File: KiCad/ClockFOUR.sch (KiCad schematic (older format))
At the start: 64 parts, among them P1 ICSP, P10 Marquee, P2 FTDI, P5 BARREL_JACK, P6 5VEN_L, P7 I2C_L, P8 5VEN_R, P9 I2C_R, SW1 SW_RST, SW2 SW_L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

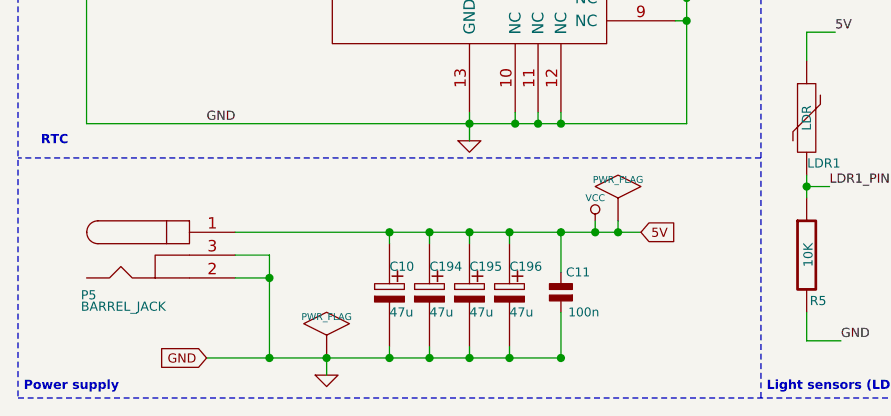
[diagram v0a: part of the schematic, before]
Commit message: C4 rev2 aka Chronogram, Sch and PCB mods, revised BoM
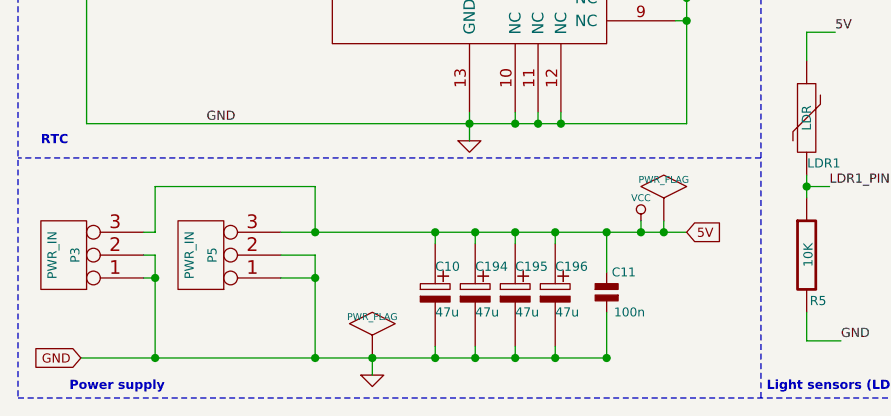
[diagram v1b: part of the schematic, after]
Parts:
- removed P5: BARREL_JACK, C4_Pretty:JACK_PJ-047a, symbol BARREL_JACK
- added P3, P5: PWR_IN, C4_Pretty:Header_3x1_PWR, symbol CONN_3
- S10, S11, S12, S13: footprint C4_Pretty:Screw_2mm -> C4_Pretty:Slot_tiewrap
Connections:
- net GND: now also P3.1, P3.2, P5.1, P5.2
- net VCC: now also P3.3, P5.3
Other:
- moved on the sheet: C10, C11, C194, C195, C196

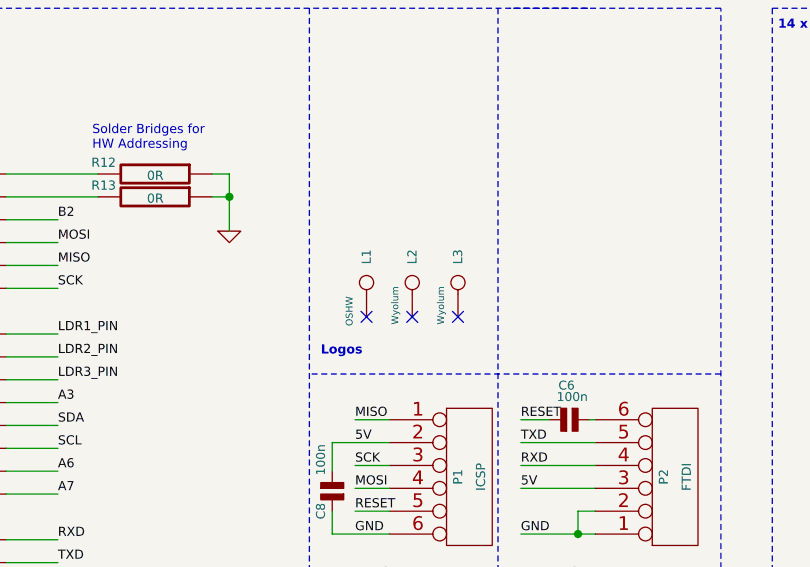
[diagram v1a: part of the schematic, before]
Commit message: Minor board tweaks
Trying to add a logo to the back of the board
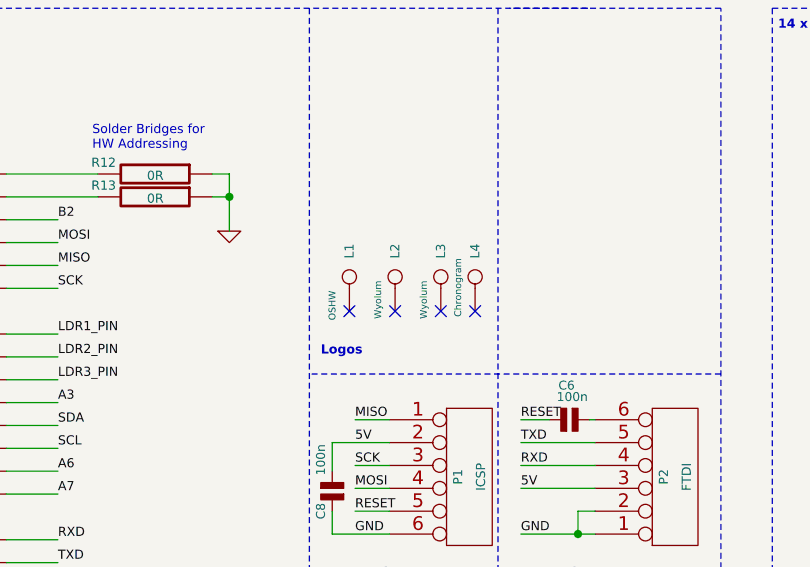
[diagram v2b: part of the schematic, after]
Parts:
- added L4: Chronogram, C4_Pretty:chronogram_dot, symbol CONN_1
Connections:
- no-connect marks 12 -> 13
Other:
- moved on the sheet: L1, L2, L3
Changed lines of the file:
@@
 C1 ED 35 72 E0 F7 FB FF F1 1F FF F1 9F FF F9 9F C7 C7 C7 73 1A 9F 2B 70 38 1C FB F6 ED 3B 79 F2
 E4 23 8F 3C 52 B0 F1 D9 2E 76 F1 FF 03 17 ED 19 47 28 92 59 FB 00 00 00 00 49 45 4E 44 AE 42 60
-82 24
+82 00
 EndData
 $EndBitmap
-NoConn ~ 5125 1900
-NoConn ~ 5325 1900
+NoConn ~ 5050 1875
+NoConn ~ 5250 1875
 $Comp
 L CONN_1 L1
 U 1 1 511CD9F8
-P 5125 1750
-F 0 "L1" H 5205 1750 40  0000 L CNN
-F 1 "OSHW" H 5000 1825 30  0000 C CNN
-F 2 "C4_Pretty:Logo_silk_OSHW_6x6mm" H 5125 1905 30  0001 C CNN
-F 3 "" H 5125 1750 60  0001 C CNN
-	1    5125 1750
+P 5050 1725
+F 0 "L1" H 5130 1725 40  0000 L CNN
+F 1 "OSHW" H 4925 1800 30  0000 C CNN
+F 2 "C4_Pretty:Logo_silk_OSHW_6x6mm" H 5050 1880 30  0001 C CNN
+F 3 "" H 5050 1725 60  0001 C CNN
+	1    5050 1725
 	0    -1   -1   0
 $EndComp
@@
 L CONN_1 L2
 U 1 1 511CD9F5
-P 5325 1750
-F 0 "L2" H 5405 1750 40  0000 L CNN
-F 1 "Wyolum" H 5225 1825 30  0000 C CNN
-F 2 "C4_Pretty:Logo-WL3" H 5250 1825 30  0001 C CNN
-F 3 "" H 5325 1750 60  0001 C CNN
-	1    5325 1750
+P 5250 1725
+F 0 "L2" H 5330 1725 40  0000 L CNN
+F 1 "Wyolum" H 5150 1800 30  0000 C CNN
+F 2 "C4_Pretty:Logo-WL3" H 5175 1800 30  0001 C CNN
+F 3 "" H 5250 1725 60  0001 C CNN
+	1    5250 1725
 	0    -1   -1   0
 $EndComp
@@
 $EndSheet
 $Comp
-L GND #PWR01
+L GND #PWR1
 U 1 1 50E7FAEA
 P 2200 7325
-F 0 "#PWR01" H 2200 7325 30  0001 C CNN
+F 0 "#PWR1" H 2200 7325 30  0001 C CNN
 F 1 "GND" H 2200 7255 30  0001 C CNN
 F 2 "" H 2200 7325 60  0001 C CNN
@@
 $EndComp
 $Comp
-L GND #PWR02
+L GND #PWR2
 U 1 1 542A3CA4
 P 2600 3975
-F 0 "#PWR02" H 2600 3975 30  0001 C CNN
+F 0 "#PWR2" H 2600 3975 30  0001 C CNN
 F 1 "GND" H 2600 3905 30  0001 C CNN
 F 2 "" H 2600 3975 60  0000 C CNN
@@
 SCL
 $Comp
-L GND #PWR03
+L GND #PWR3
 U 1 1 542BA28D
 P 2625 6300
-F 0 "#PWR03" H 2625 6300 30  0001 C CNN
+F 0 "#PWR3" H 2625 6300 30  0001 C CNN
 F 1 "GND" H 2625 6230 30  0001 C CNN
 F 2 "" H 2625 6300 60  0000 C CNN
@@
 RESET
 $Comp
-L PWR_FLAG #FLG04
+L PWR_FLAG #FLG1
 U 1 1 542A828E
 P 950 4450
-F 0 "#FLG04" H 950 4720 30  0001 C CNN
+F 0 "#FLG1" H 950 4720 30  0001 C CNN
 F 1 "PWR_FLAG" H 950 4680 30  0000 C CNN
 F 2 "" H 950 4450 60  0000 C CNN
@@
 SCK
 $Comp
-L PWR_FLAG #FLG05
+L PWR_FLAG #FLG3
 U 1 1 542C2187
 P 3475 6650
-F 0 "#FLG05" H 3475 6745 30  0001 C CNN
+F 0 "#FLG3" H 3475 6745 30  0001 C CNN
 F 1 "PWR_FLAG" H 3475 6830 30  0000 C CNN
 F 2 "" H 3475 6650 60  0000 C CNN
@@
 $EndComp
 $Comp
-L PWR_FLAG #FLG06
+L PWR_FLAG #FLG2
 U 1 1 542C219E
 P 2200 7250
-F 0 "#FLG06" H 2200 7345 30  0001 C CNN
+F 0 "#FLG2" H 2200 7345 30  0001 C CNN
 F 1 "PWR_FLAG" H 2200 7430 30  0000 C CNN
 F 2 "" H 2200 7250 60  0000 C CNN
@@
 $EndComp
 $Comp
-L VCC #PWR07
+L VCC #PWR4
 U 1 1 542BE803
 P 3375 6650
-F 0 "#PWR07" H 3375 6750 30  0001 C CNN
+F 0 "#PWR4" H 3375 6750 30  0001 C CNN
 F 1 "VCC" H 3375 6750 30  0000 C CNN
 F 2 "" H 3375 6650 60  0000 C CNN
@@
 Text Label 5625 4900 2    40   ~ 0
 SW_R
-NoConn ~ 5525 1900
+NoConn ~ 5450 1875
 $Comp
 L CONN_1 L3
 U 1 1 5439906B
-P 5525 1750
-F 0 "L3" H 5605 1750 40  0000 L CNN
-F 1 "Wyolum" H 5425 1825 30  0000 C CNN
-F 2 "C4_Pretty:Logo-WL3" H 5450 1825 30  0001 C CNN
-F 3 "" H 5525 1750 60  0001 C CNN
-	1    5525 1750
+P 5450 1725
+F 0 "L3" H 5530 1725 40  0000 L CNN
+F 1 "Wyolum" H 5350 1800 30  0000 C CNN
+F 2 "C4_Pretty:Logo-WL3" H 5375 1800 30  0001 C CNN
+F 3 "" H 5450 1725 60  0001 C CNN
+	1    5450 1725
 	0    -1   -1   0
 $EndComp
@@
 $EndComp
 $Comp
-L GND #PWR08
+L GND #PWR5
 U 1 1 5439D79A
 P 4525 1525
-F 0 "#PWR08" H 4525 1525 30  0001 C CNN
+F 0 "#PWR5" H 4525 1525 30  0001 C CNN
 F 1 "GND" H 4525 1455 30  0001 C CNN
 F 2 "" H 4525 1525 60  0000 C CNN
@@
 	1950 6500 1950 6700
 Connection ~ 1950 6700
+NoConn ~ 5600 1875
+$Comp
+L CONN_1 L4
+U 1 1 54C81555
+P 5600 1725
+F 0 "L4" H 5680 1725 40  0000 L CNN
+F 1 "Chronogram" H 5425 1800 30  0000 L CNN
+F 2 "C4_Pretty:chronogram_dot" H 5600 1880 30  0001 C CNN
+F 3 "" H 5600 1725 60  0001 C CNN
+	1    5600 1725
+	0    -1   -1   0
+$EndComp
 $EndSCHEMATC

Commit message: Added Fuse/Zener protection, silk legend mods
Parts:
- added D1: SMBJ5339B, C4_Pretty:diode-DO214AA, symbol DIODE_ZENER
- added F1: miniSMDC200F/16, C4_Pretty:f_1812, symbol FUSE
- L1, L2, L3: symbol CONN_1 -> Logos
- L4: footprint C4_Pretty:chronogram_dot -> C4_Pretty:Logo_silk_OSHW_6x6mm; symbol CONN_1 -> Logos
- LDR1, LDR2, LDR3: footprint C4_Pretty:r_0805 -> C4_Pretty:r_0805_ldr
- SW2: Label (none) -> Mode
- SW3: Label (none) -> Color
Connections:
- net GND: now also D1.1 (A)
- net VCC: now also D1.2 (K), F1.2; no longer P3.3, P5.3
- new net: F1.1, P3.3, P5.3
- no-connect marks 13 -> 9
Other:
- moved on the sheet: P3, P5
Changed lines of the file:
@@
 EESchema Schematic File Version 2
 LIBS:ClockFOUR
+LIBS:device
 LIBS:ClockFOUR-cache
 EELAYER 25 0
@@
 C1 ED 35 72 E0 F7 FB FF F1 1F FF F1 9F FF F9 9F C7 C7 C7 73 1A 9F 2B 70 38 1C FB F6 ED 3B 79 F2
 E4 23 8F 3C 52 B0 F1 D9 2E 76 F1 FF 03 17 ED 19 47 28 92 59 FB 00 00 00 00 49 45 4E 44 AE 42 60
-82 00
+82 B7
 EndData
 $EndBitmap
-NoConn ~ 5050 1875
-NoConn ~ 5250 1875
-$Comp
-L CONN_1 L1
+$Comp
+L Logos L1
 U 1 1 511CD9F8
 P 5050 1725
@@
 $EndComp
 $Comp
-L CONN_1 L2
+L Logos L2
 U 1 1 511CD9F5
 P 5250 1725
@@
 	0    -1   -1   0
 $EndComp
-Text GLabel 925  7250 0    40   Input ~ 0
+Text GLabel 850  7250 0    40   Input ~ 0
 GND
-Text GLabel 3575 6700 2    40   Input ~ 0
+Text GLabel 3300 6700 2    40   Input ~ 0
 5V
 $Sheet
@@
 $EndSheet
 $Comp
-L GND #PWR1
+L GND #PWR01
 U 1 1 50E7FAEA
-P 2200 7325
-F 0 "#PWR1" H 2200 7325 30  0001 C CNN
-F 1 "GND" H 2200 7255 30  0001 C CNN
-F 2 "" H 2200 7325 60  0001 C CNN
-F 3 "" H 2200 7325 60  0001 C CNN
-	1    2200 7325
+P 2250 7325
+F 0 "#PWR01" H 2250 7325 30  0001 C CNN
+F 1 "GND" H 2250 7255 30  0001 C CNN
+F 2 "" H 2250 7325 60  0001 C CNN
+F 3 "" H 2250 7325 60  0001 C CNN
+	1    2250 7325
 	1    0    0    -1
 $EndComp
@@
 $EndComp
 $Comp
-L GND #PWR2
+L GND #PWR02
 U 1 1 542A3CA4
 P 2600 3975
-F 0 "#PWR2" H 2600 3975 30  0001 C CNN
+F 0 "#PWR02" H 2600 3975 30  0001 C CNN
 F 1 "GND" H 2600 3905 30  0001 C CNN
 F 2 "" H 2600 3975 60  0000 C CNN
@@
 SCL
 $Comp
-L GND #PWR3
+L GND #PWR03
 U 1 1 542BA28D
 P 2625 6300
-F 0 "#PWR3" H 2625 6300 30  0001 C CNN
+F 0 "#PWR03" H 2625 6300 30  0001 C CNN
 F 1 "GND" H 2625 6230 30  0001 C CNN
 F 2 "" H 2625 6300 60  0000 C CNN
@@
 P 3225 6975
 F 0 "C11" H 3300 7075 39  0000 C CNN
-F 1 "100n" H 3325 6900 39  0000 C CNN
+F 1 "100n" H 3375 7000 39  0000 C CNN
 F 2 "C4_Pretty:c_0805" H 3225 6975 60  0001 C CNN
 F 3 "" H 3225 6975 60  0000 C CNN
@@
 RESET
 $Comp
-L PWR_FLAG #FLG1
+L PWR_FLAG #FLG04
 U 1 1 542A828E
 P 950 4450
-F 0 "#FLG1" H 950 4720 30  0001 C CNN
+F 0 "#FLG04" H 950 4720 30  0001 C CNN
 F 1 "PWR_FLAG" H 950 4680 30  0000 C CNN
 F 2 "" H 950 4450 60  0000 C CNN
@@
 SCK
 $Comp
-L PWR_FLAG #FLG3
+L PWR_FLAG #FLG05
 U 1 1 542C2187
-P 3475 6650
-F 0 "#FLG3" H 3475 6745 30  0001 C CNN
-F 1 "PWR_FLAG" H 3475 6830 30  0000 C CNN
-F 2 "" H 3475 6650 60  0000 C CNN
-F 3 "" H 3475 6650 60  0000 C CNN
-	1    3475 6650
-	1    0    0    -1
-$EndComp
-$Comp
-L PWR_FLAG #FLG2
+P 3225 6650
+F 0 "#FLG05" H 3225 6745 30  0001 C CNN
+F 1 "PWR_FLAG" H 3225 6830 30  0000 C CNN
+F 2 "" H 3225 6650 60  0000 C CNN
+F 3 "" H 3225 6650 60  0000 C CNN
+	1    3225 6650
+	1    0    0    -1
+$EndComp
+$Comp
+L PWR_FLAG #FLG06
 U 1 1 542C219E
-P 2200 7250
-F 0 "#FLG2" H 2200 7345 30  0001 C CNN
-F 1 "PWR_FLAG" H 2200 7430 30  0000 C CNN
-F 2 "" H 2200 7250 60  0000 C CNN
-F 3 "" H 2200 7250 60  0000 C CNN
-	1    2200 7250
+P 3375 7225
+F 0 "#FLG06" H 3375 7320 30  0001 C CNN
+F 1 "PWR_FLAG" H 3375 7405 30  0000 C CNN
+F 2 "" H 3375 7225 60  0000 C CNN
+F 3 "" H 3375 7225 60  0000 C CNN
+	1    3375 7225
 	1    0    0    -1
 $EndComp
@@
 $EndComp
 $Comp
-L VCC #PWR4
+L VCC #PWR07
 U 1 1 542BE803
-P 3375 6650
-F 0 "#PWR4" H 3375 6750 30  0001 C CNN
-F 1 "VCC" H 3375 6750 30  0000 C CNN
-F 2 "" H 3375 6650 60  0000 C CNN
-F 3 "" H 3375 6650 60  0000 C CNN
-	1    3375 6650
+P 3000 6550
+F 0 "#PWR07" H 3000 6650 30  0001 C CNN
+F 1 "VCC" H 3000 6650 30  0000 C CNN
+F 2 "" H 3000 6550 60  0000 C CNN
+F 3 "" H 3000 6550 60  0000 C CNN
+	1    3000 6550
 	1    0    0    -1
 $EndComp
@@
 F 2 "C4_Pretty:SW_SMD" H 5075 4575 60  0001 C CNN
 F 3 "~" H 5075 4575 60  0000 C CNN
+F 4 "Mode" H 5075 4700 40  0000 C CNN "Label"
 	1    5075 4575
 	0    -1   1    0
@@
 F 2 "C4_Pretty:SW_SMD" H 5425 4575 60  0001 C CNN
 F 3 "~" H 5425 4575 60  0000 C CNN
+F 4 "Color" H 5425 4700 40  0000 C CNN "Label"
 	1    5425 4575
 	0    -1   1    0
@@
 Text Label 5625 4900 2    40   ~ 0
 SW_R
-NoConn ~ 5450 1875
-$Comp
-L CONN_1 L3
+$Comp
+L Logos L3
 U 1 1 5439906B
 P 5450 1725
@@
 $EndComp
 $Comp
-L GND #PWR5
+L GND #PWR08
 U 1 1 5439D79A
 P 4525 1525
-F 0 "#PWR5" H 4525 1525 30  0001 C CNN
+F 0 "#PWR08" H 4525 1525 30  0001 C CNN
 F 1 "GND" H 4525 1455 30  0001 C CNN
 F 2 "" H 4525 1525 60  0000 C CNN
@@
 Wire Wire Line
 	1650 1725 750  1725
-Connection ~ 1950 7250
-Wire Wire Line
-	1950 6800 1950 7250
-Wire Wire Line
-	1800 6800 1950 6800
-Wire Wire Line
-	925  7250 3225 7250
-Wire Wire Line
-	2200 7250 2200 7325
+Connection ~ 1750 7250
+Wire Wire Line
+	1750 7250 1750 6800
+Wire Wire Line
+	1750 6800 1700 6800
+Wire Wire Line
+	850  7250 3375 7250
 Wire Wire Line
 	875  3150 875  3050
 Wire Wire Line
 	875  2150 875  2275
-Connection ~ 2200 7250
+Connection ~ 2250 7250
 Wire Wire Line
 	2625 4350 2625 4525
@@
 	4875 3075 6675 3075
 Wire Wire Line
-	3225 6700 3225 6875
+	3225 6650 3225 6875
 Wire Wire Line
 	3225 7250 3225 7050
@@
 Wire Wire Line
 	2475 6700 2475 6750
-Connection ~ 2475 6700
 Wire Wire Line
 	2650 6700 2650 6750
@@
 Connection ~ 2825 6700
 Wire Wire Line
-	3000 6700 3000 6750
+	3000 6550 3000 6750
 Connection ~ 3000 6700
 Wire Wire Line
@@
 	3900 6375 650  6375
 Wire Wire Line
-	3475 6700 3475 6650
-Wire Wire Line
-	1800 6700 3575 6700
+	1700 6700 1775 6700
+Wire Wire Line
+	2175 6700 3300 6700
 Connection ~ 3225 6700
-Connection ~ 3475 6700
-Wire Wire Line
-	3375 6650 3375 6700
-Connection ~ 3375 6700
 Wire Notes Line
 	6900 5350 9200 5350
@@
 F 0 "LDR1" H 4175 6025 40  0000 C TNN
 F 1 "LDR" V 4100 6200 40  0000 C CNN
-F 2 "C4_Pretty:r_0805" H 4100 6200 60  0001 C CNN
+F 2 "C4_Pretty:r_0805_ldr" H 4100 6200 60  0001 C CNN
 F 3 "~" H 4100 6200 60  0000 C CNN
 	1    4100 6200
@@
 F 0 "LDR2" H 4675 6025 40  0000 C TNN
 F 1 "LDR" V 4600 6200 40  0000 C CNN
-F 2 "C4_Pretty:r_0805" H 4600 6200 60  0001 C CNN
+F 2 "C4_Pretty:r_0805_ldr" H 4600 6200 60  0001 C CNN
 F 3 "~" H 4600 6200 60  0000 C CNN
 	1    4600 6200
@@
 F 0 "LDR3" H 5175 6025 40  0000 C TNN
 F 1 "LDR" V 5100 6200 40  0000 C CNN
-F 2 "C4_Pretty:r_0805" H 5100 6200 60  0001 C CNN
+F 2 "C4_Pretty:r_0805_ldr" H 5100 6200 60  0001 C CNN
 F 3 "~" H 5100 6200 60  0000 C CNN
 	1    5100 6200
@@
 L CONN_3 P5
 U 1 1 54C50337
-P 1450 6800
-F 0 "P5" V 1400 6800 40  0000 C CNN
-F 1 "PWR_IN" V 1500 6800 40  0000 C CNN
-F 2 "C4_Pretty:Header_3x1_PWR" H 1450 6650 60  0001 C CNN
-F 3 "" H 1450 6650 60  0000 C CNN
-	1    1450 6800
+P 1350 6800
+F 0 "P5" V 1300 6800 40  0000 C CNN
+F 1 "PWR_IN" V 1400 6800 40  0000 C CNN
+F 2 "C4_Pretty:Header_3x1_PWR" H 1350 6650 60  0001 C CNN
+F 3 "" H 1350 6650 60  0000 C CNN
+	1    1350 6800
 	-1   0    0    1
 $EndComp
 Wire Wire Line
-	1800 6900 1950 6900
-Connection ~ 1950 6900
+	1700 6900 1750 6900
+Connection ~ 1750 6900
 $Comp
 L CONN_3 P3
 U 1 1 54C53C4F
-P 850 6800
-F 0 "P3" V 800 6800 40  0000 C CNN
-F 1 "PWR_IN" V 900 6800 40  0000 C CNN
-F 2 "C4_Pretty:Header_3x1_PWR" H 850 6650 60  0001 C CNN
-F 3 "" H 850 6650 60  0000 C CNN
-	1    850  6800
+P 775 6800
+F 0 "P3" V 725 6800 40  0000 C CNN
+F 1 "PWR_IN" V 825 6800 40  0000 C CNN
+F 2 "C4_Pretty:Header_3x1_PWR" H 775 6650 60  0001 C CNN
+F 3 "" H 775 6650 60  0000 C CNN
+	1    775  6800
 	-1   0    0    1
 $EndComp
 Wire Wire Line
-	1200 6800 1250 6800
-Wire Wire Line
-	1250 6800 1250 7250
-Connection ~ 1250 7250
-Wire Wire Line
-	1200 6900 1250 6900
-Connection ~ 1250 6900
-Wire Wire Line
-	1200 6700 1250 6700
-Wire Wire Line
-	1250 6700 1250 6500
-Wire Wire Line
-	1250 6500 1950 6500
-Wire Wire Line
-	1950 6500 1950 6700
-Connection ~ 1950 6700
-NoConn ~ 5600 1875
-$Comp
-L CONN_1 L4
+	1125 6800 1175 6800
+Wire Wire Line
+	1175 6800 1175 7250
+Connection ~ 1175 7250
+Wire Wire Line
+	1125 6900 1175 6900
+Connection ~ 1175 6900
+Wire Wire Line
+	1125 6700 1175 6700
+Wire Wire Line
+	1175 6700 1175 6500
+Wire Wire Line
+	1175 6500 1750 6500
+Wire Wire Line
+	1750 6500 1750 6700
+$Comp
+L Logos L4
 U 1 1 54C81555
 P 5600 1725
 F 0 "L4" H 5680 1725 40  0000 L CNN
 F 1 "Chronogram" H 5425 1800 30  0000 L CNN
-F 2 "C4_Pretty:chronogram_dot" H 5600 1880 30  0001 C CNN
+F 2 "C4_Pretty:Logo_silk_OSHW_6x6mm" H 5600 1880 30  0001 C CNN
 F 3 "" H 5600 1725 60  0001 C CNN
 	1    5600 1725
 	0    -1   -1   0
 $EndComp
+Wire Wire Line
+	3375 7250 3375 7225
+$Comp
+L DIODE_ZENER D1
+U 1 1 54C80AA6
+P 2250 6975
+F 0 "D1" V 2250 7075 50  0000 C CNN
+F 1 "SMBJ5339B" H 2250 6875 40  0000 C CNN
+F 2 "C4_Pretty:diode-DO214AA" H 2075 7000 60  0001 C CNN
+F 3 "" H 2075 7000 60  0000 C CNN
+	1    2250 6975
+	0    -1   -1   0
+$EndComp
+$Comp
+L FUSE F1
+U 1 1 54C80AE5
+P 1975 6700
+F 0 "F1" H 2000 6600 40  0000 C CNN
+F 1 "miniSMDC200F/16" H 2100 6800 40  0000 C CNN
+F 2 "C4_Pretty:f_1812" H 1975 6700 60  0001 C CNN
+F 3 "" H 1975 6700 60  0000 C CNN
+	1    1975 6700
+	1    0    0    -1
+$EndComp
+Connection ~ 1750 6700
+Connection ~ 2475 6700
+Wire Wire Line
+	2250 7175 2250 7325
+Wire Wire Line
+	2250 6775 2250 6700
+Connection ~ 2250 6700
 $EndSCHEMATC
